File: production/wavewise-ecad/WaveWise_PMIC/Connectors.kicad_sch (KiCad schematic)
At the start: 7 parts, among them J10 Signals output, J11 Servo output, J12 Regulated 48V Input, J13 Panel Input, J14 Battery Direct Input, J15 GNDs, J4 Power outputs

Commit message: add control stuff
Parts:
- removed J4: Power outputs, symbol Connector:Screw_Terminal_01x03
- added J1: Power Outputs, symbol Connector:Screw_Terminal_01x03
- added J2: Inverter Inputs, symbol Connector:Screw_Terminal_01x02
- added J3: 5031590300, CON_5031590300_MOL, symbol 3pinmolex:5031590300
- added J5: 5031590400, CON_5031590400_MOL, symbol 4pinmolex:5031590400
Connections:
- net +12V: now also J1.2 (Pin_2)
- net +24V: now also J1.3 (Pin_3)
- net +5V: now also J1.1 (Pin_1)
- net GND: now also J2.1 (Pin_1), J3.2
- new net AOUT1: J5.1
- new net AOUT2: J5.2
- new net BOUT1: J5.3
- new net BOUT2: J5.4
- new net CLK: J3.1
- new net DIO: J3.3
- new net Inverter_Input: J2.2 (Pin_2)
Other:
- note added: "MCU Debug"
- note added: "Motor Controller"
- moved on the sheet: J15

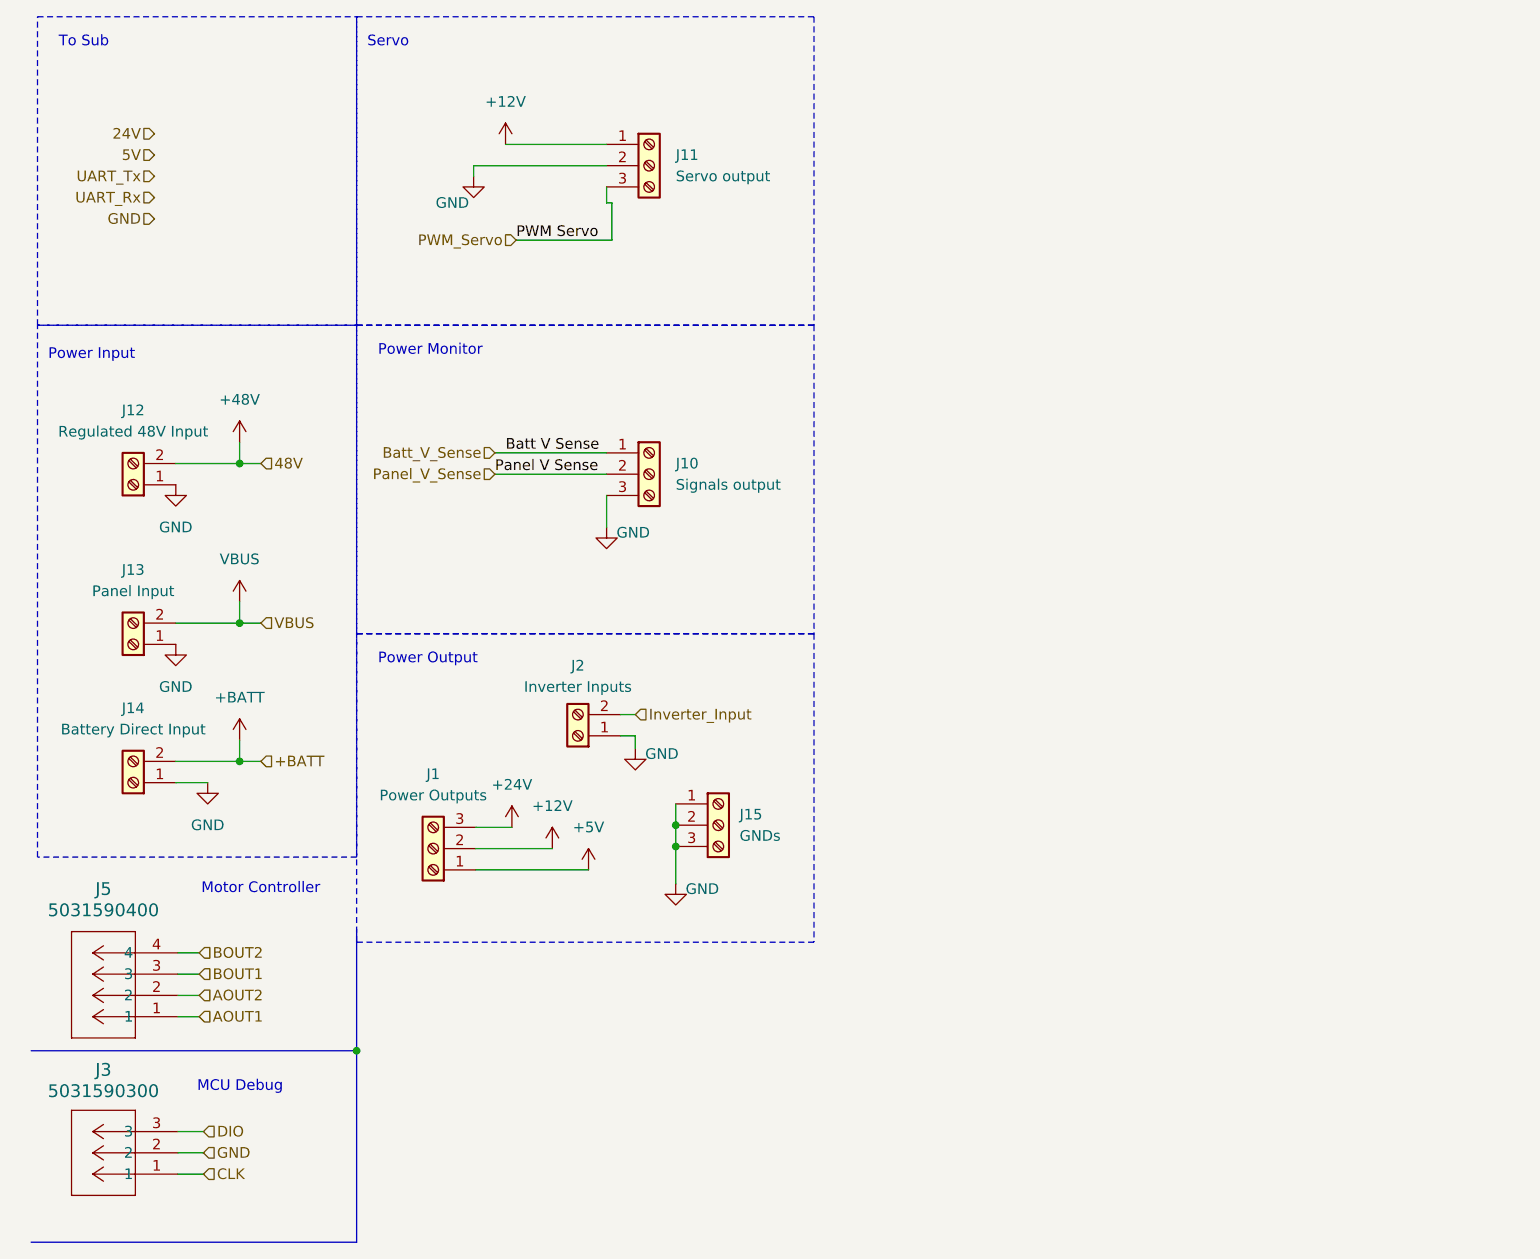
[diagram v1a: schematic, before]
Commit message: updated root and adding connectors
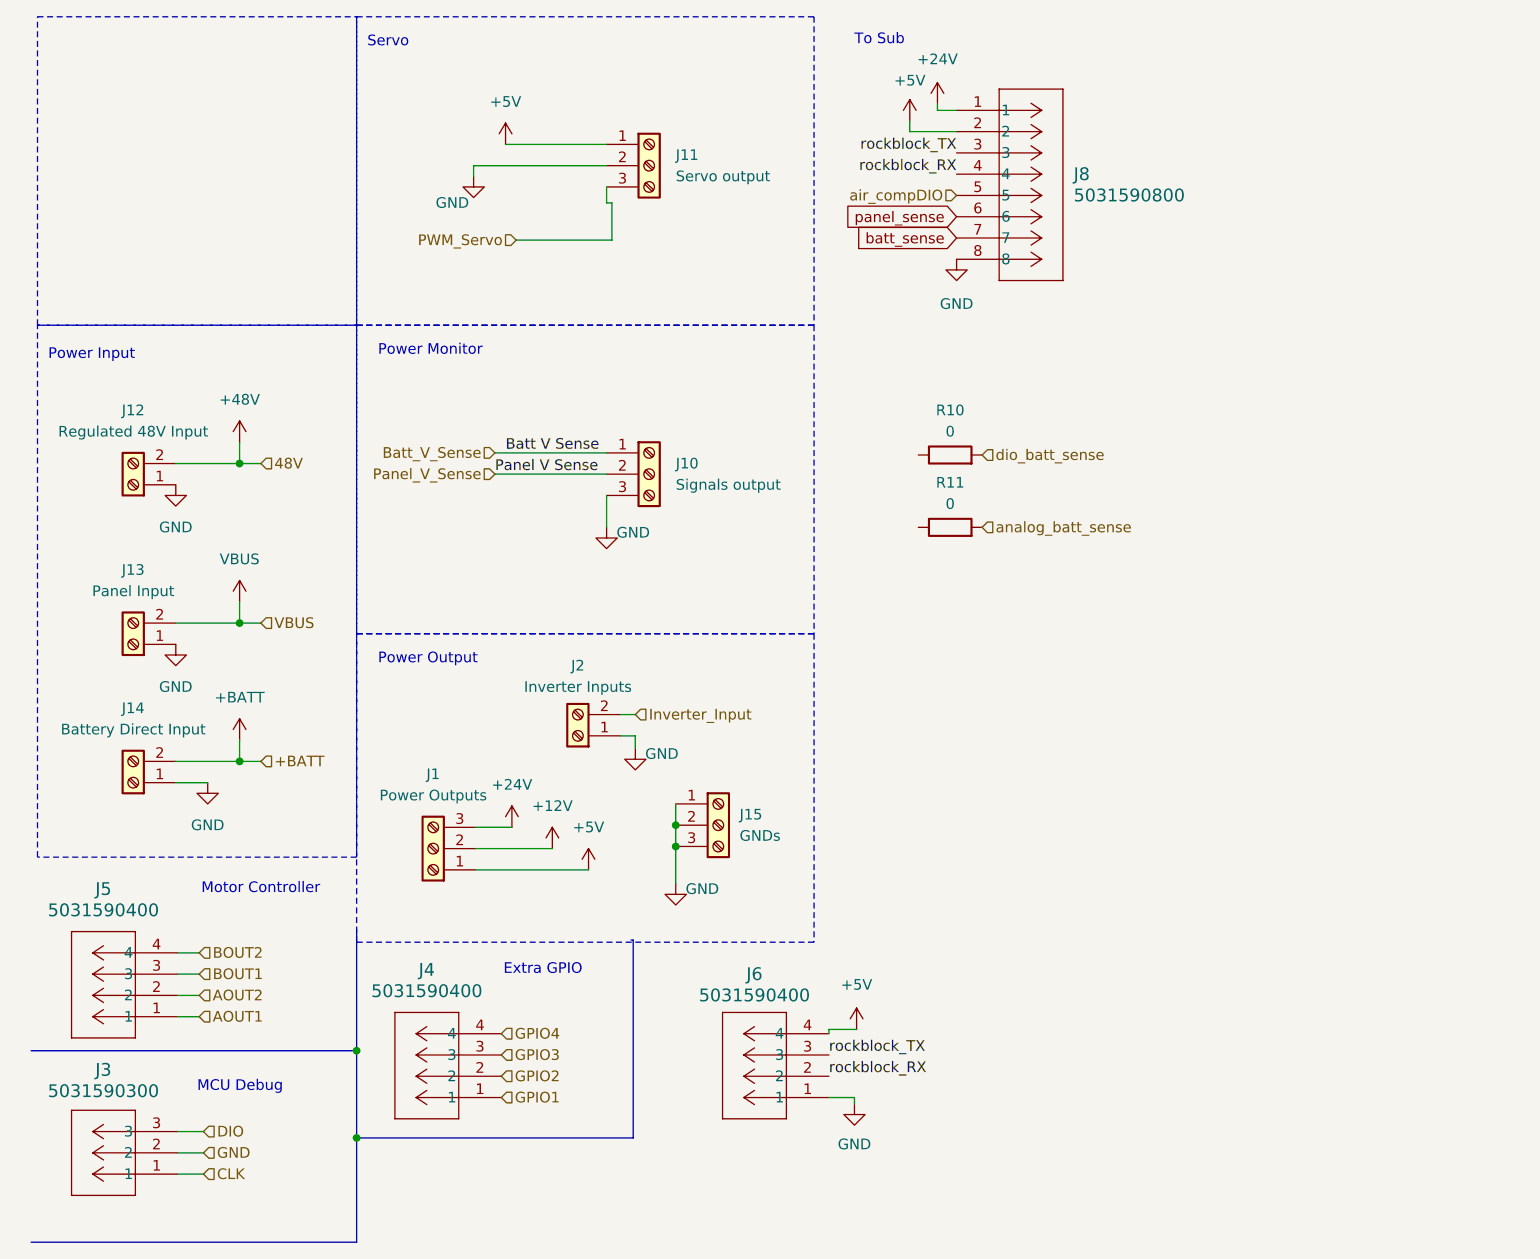
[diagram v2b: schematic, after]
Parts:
- added J4, J6: 5031590400, CON_5031590400_MOL, symbol 4pinmolex:5031590400
- added J8: 5031590800, CON_5031590800_MOL, symbol 8pinmolex:5031590800
- added R10, R11: 0, Resistor_SMD:R_0805_2012Metric, symbol Device:R
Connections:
- net +12V: no longer J11.1 (Pin_1)
- net +24V: now also J8.1
- net +5V: now also J11.1 (Pin_1), J6.4, J8.2
- net GND: now also J6.1, J8.8
- new net GPIO1: J4.1
- new net GPIO2: J4.2
- new net GPIO3: J4.3
- new net GPIO4: J4.4
- new net air_compDIO: J8.5
- new net analog_batt_sense: R11.2
- new net batt_sense: J8.7
- new net dio_batt_sense: R10.2
- new net panel_sense: J8.6
- new net rockblock_RX: J6.2, J8.4
- new net rockblock_TX: J6.3, J8.3
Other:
- note added: "Extra GPIO"

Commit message: adding more to root page and updating for battery sensing
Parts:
- added R12, R13: 0, Resistor_SMD:R_0805_2012Metric, symbol Device:R
- R11: now not fitted
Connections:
- net batt_sense: now also R10.1, R11.1
- net panel_sense: now also R12.1, R13.1
- net rockblock_RX: no longer J6.2
- net rockblock_TX: no longer J6.3
- net air_compDIO renamed air_comp_dio
- net analog_batt_sense renamed Batt_V_sense
- new net Panel_V_sense: R13.2
- new net dio_panel_sense: R12.2
- new net rockblock_RX_conn: J6.2
- new net rockblock_TX_conn: J6.3
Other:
- note added: "Output for panel/battery sensing (unsure if using analog or digital yet)"
- note added: "Rockblock Power Connection"
- moved on the sheet: J4, J6, R10

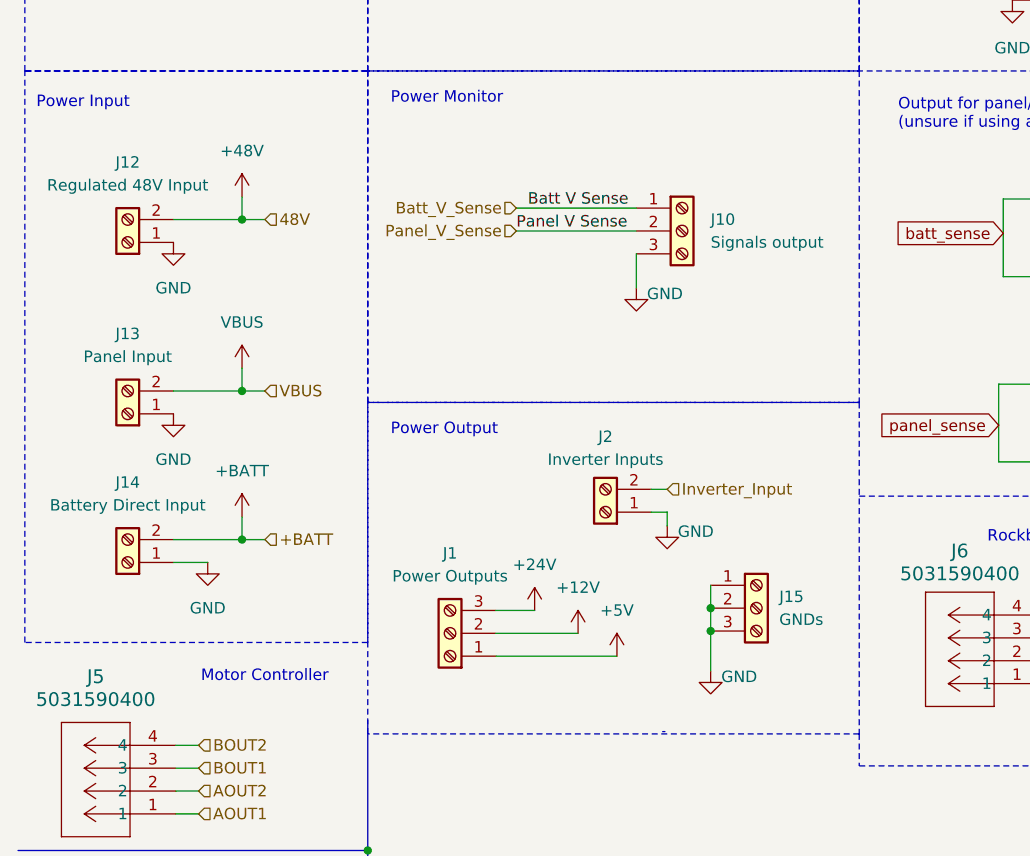
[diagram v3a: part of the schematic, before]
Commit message: added most footprints still need polulu footprint
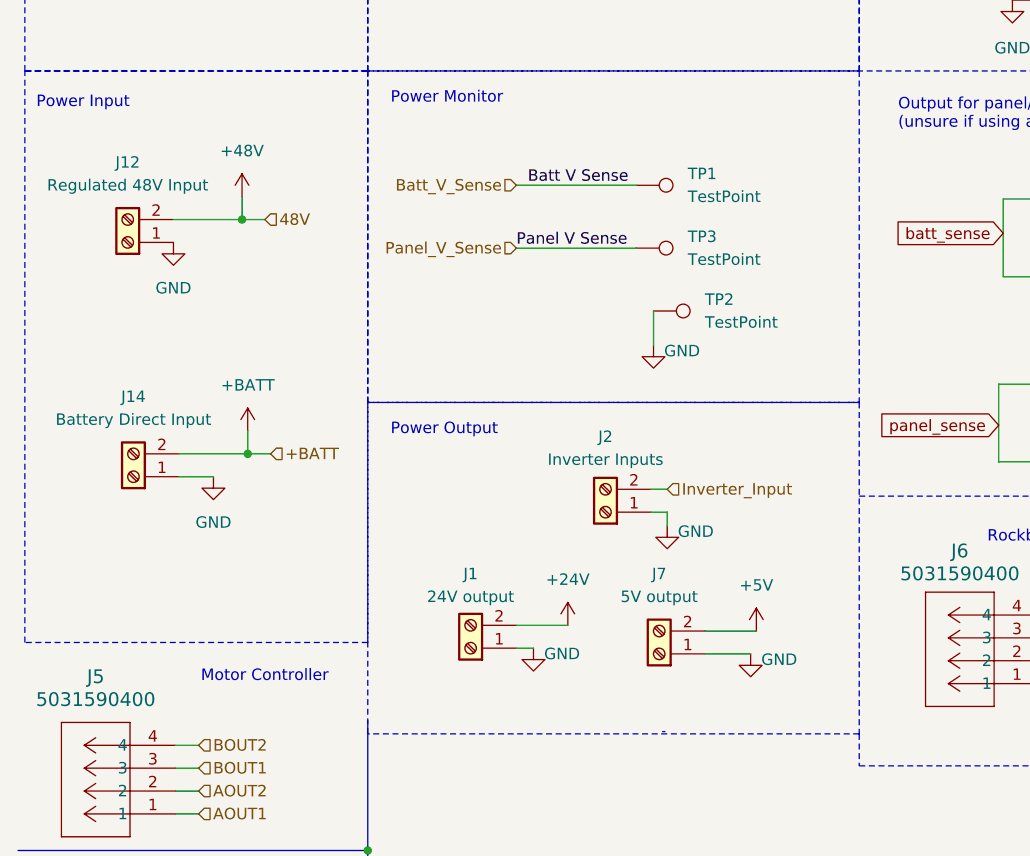
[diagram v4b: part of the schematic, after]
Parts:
- removed J10: Signals output, symbol Connector:Screw_Terminal_01x03
- removed J13: Panel Input, symbol Connector:Screw_Terminal_01x02
- removed J15: GNDs, symbol Connector:Screw_Terminal_01x03
- added J7: 5V output, Unchecked:2pinmolex, symbol Connector:Screw_Terminal_01x02
- added TP1, TP3: TestPoint, TestPoint:TestPoint_Pad_1.0x1.0mm, symbol Connector:TestPoint
- added TP2: TestPoint, TestPoint:TestPoint_Pad_1.5x1.5mm, symbol Connector:TestPoint
- J1: value Power Outputs -> 24V output; footprint (none) -> Unchecked:2pinmolex; symbol Connector:Screw_Terminal_01x03 -> Connector:Screw_Terminal_01x02
- J12, J14, J2: footprint (none) -> Unchecked:1731721
- J3: footprint CON_5031590300_MOL -> Unchecked:3pinmolex
- J4, J5, J6: footprint CON_5031590400_MOL -> Footprints:4pinmolex
- J8: footprint CON_5031590800_MOL -> Footprints:8pinmolex
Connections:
- net +12V is gone; now on net +24V: J1.2 (Pin_2)
- net +24V: no longer J1.3 (Pin_3)
- net +5V: now also J7.2 (Pin_2); no longer J1.1 (Pin_1)
- net Batt_V_Sense: now also TP1.1
- net GND: now also J1.1 (Pin_1), J7.1 (Pin_1), TP2.1
- net Panel_V_Sense: now also TP3.1
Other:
- moved on the sheet: J14

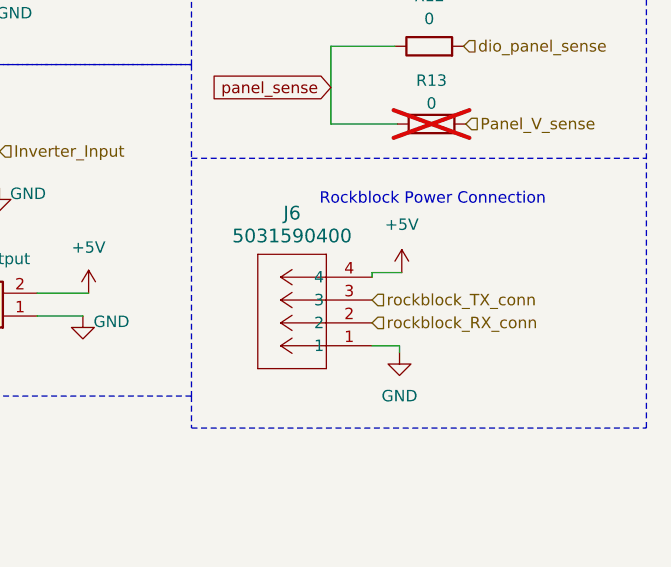
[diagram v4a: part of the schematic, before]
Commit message: More stuff done to PCB Added polulu
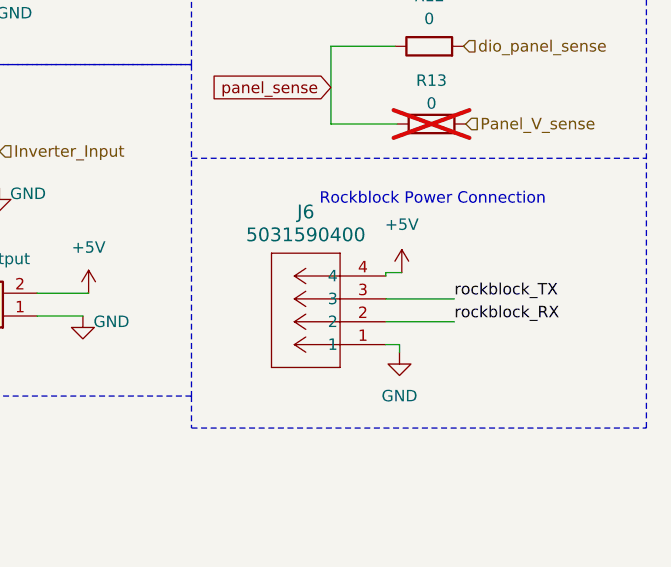
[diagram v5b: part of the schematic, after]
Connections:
- net rockblock_RX_conn is gone; now on net rockblock_RX: J6.2
- net rockblock_TX_conn is gone; now on net rockblock_TX: J6.3
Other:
- moved on the sheet: J6
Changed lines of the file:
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@@
     (stroke (width 0) (type default))
   )
-  (wire (pts (xy 128.778 109.474) (xy 125.476 109.474))
+  (wire (pts (xy 128.778 109.474) (xy 127 109.474))
     (stroke (width 0) (type default))
   )
@@
     (stroke (width 0) (type default))
   )
+  (wire (pts (xy 127 112.395) (xy 134.62 112.395))
+    (stroke (width 0) (type default))
+  )
   (wire (pts (xy 120.142 23.114) (xy 120.142 23.876))
     (stroke (width 0) (type default))
   )
+  (wire (pts (xy 134.62 114.935) (xy 127 114.935))
+    (stroke (width 0) (type default))
+  )
   (wire (pts (xy 29.21 66.04) (xy 36.83 66.04))
     (stroke (width 0) (type default))
@@
     (stroke (width 0) (type default))
   )
-  (wire (pts (xy 125.476 117.602) (xy 128.524 117.602))
+  (wire (pts (xy 127 117.475) (xy 128.524 117.475))
     (stroke (width 0) (type default))
   )
@@
     (stroke (width 0) (type default))
   )
-  (wire (pts (xy 128.524 117.602) (xy 128.524 118.364))
+  (wire (pts (xy 128.524 117.475) (xy 128.524 118.364))
     (stroke (width 0) (type default))
   )
@@
     (stroke (width 0.15) (type dash))
   )
-  (wire (pts (xy 125.476 109.474) (xy 125.476 109.982))
+  (wire (pts (xy 127 109.474) (xy 127 109.855))
     (stroke (width 0) (type default))
   )
@@
     (effects (font (size 1.27 1.27)) (justify left bottom))
   )
+  (label "rockblock_RX" (at 134.62 114.935 0) (fields_autoplaced)
+    (effects (font (size 1.27 1.27)) (justify left bottom))
+  )
   (label "Panel V Sense" (at 67.31 69.215 0) (fields_autoplaced)
     (effects (font (size 1.27 1.27)) (justify left bottom))
@@
     (effects (font (size 1.27 1.27)) (justify right bottom))
   )
+  (label "rockblock_TX" (at 134.62 112.395 0) (fields_autoplaced)
+    (effects (font (size 1.27 1.27)) (justify left bottom))
+  )
   (global_label "batt_sense" (shape input) (at 121.412 67.564 180) (fields_autoplaced)
     (effects (font (size 1.27 1.27)) (justify right))
@@
     (effects (font (size 1.27 1.27)) (justify right))
   )
-  (hierarchical_label "rockblock_TX_conn" (shape input) (at 125.476 112.522 0) (fields_autoplaced)
-    (effects (font (size 1.27 1.27)) (justify left))
-  )
   (hierarchical_label "Panel_V_sense" (shape input) (at 135.89 92.964 0) (fields_autoplaced)
     (effects (font (size 1.27 1.27)) (justify left))
   )
   (hierarchical_label "Inverter_Input" (shape input) (at 84.074 96.012 0) (fields_autoplaced)
-    (effects (font (size 1.27 1.27)) (justify left))
-  )
-  (hierarchical_label "rockblock_RX_conn" (shape input) (at 125.476 115.062 0) (fields_autoplaced)
     (effects (font (size 1.27 1.27)) (justify left))
   )
@@
     )
   )
-  (symbol (lib_id "4pinmolex:5031590400") (at 125.476 117.602 180) (unit 1)
-    (in_bom yes) (on_board yes) (dnp no) (fields_autoplaced)
-    (property "Reference" "J6" (at 116.586 102.87 0)
+  (symbol (lib_id "4pinmolex:5031590400") (at 127 117.475 180) (unit 1)
+    (in_bom yes) (on_board yes) (dnp no) (fields_autoplaced)
+    (property "Reference" "J6" (at 118.11 102.743 0)
       (effects (font (size 1.524 1.524)))
     )
-    (property "Value" "5031590400" (at 116.586 105.41 0)
+    (property "Value" "5031590400" (at 118.11 105.283 0)
       (effects (font (size 1.524 1.524)))
     )
-    (property "Footprint" "Footprints:4pinmolex" (at 125.476 117.602 0)
+    (property "Footprint" "Footprints:4pinmolex" (at 127 117.475 0)
       (effects (font (size 1.27 1.27) italic) hide)
     )
-    (property "Datasheet" "5031590400" (at 125.476 117.602 0)
+    (property "Datasheet" "5031590400" (at 127 117.475 0)
       (effects (font (size 1.27 1.27) italic) hide)
     )
